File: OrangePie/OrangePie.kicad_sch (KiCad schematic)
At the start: 0 parts

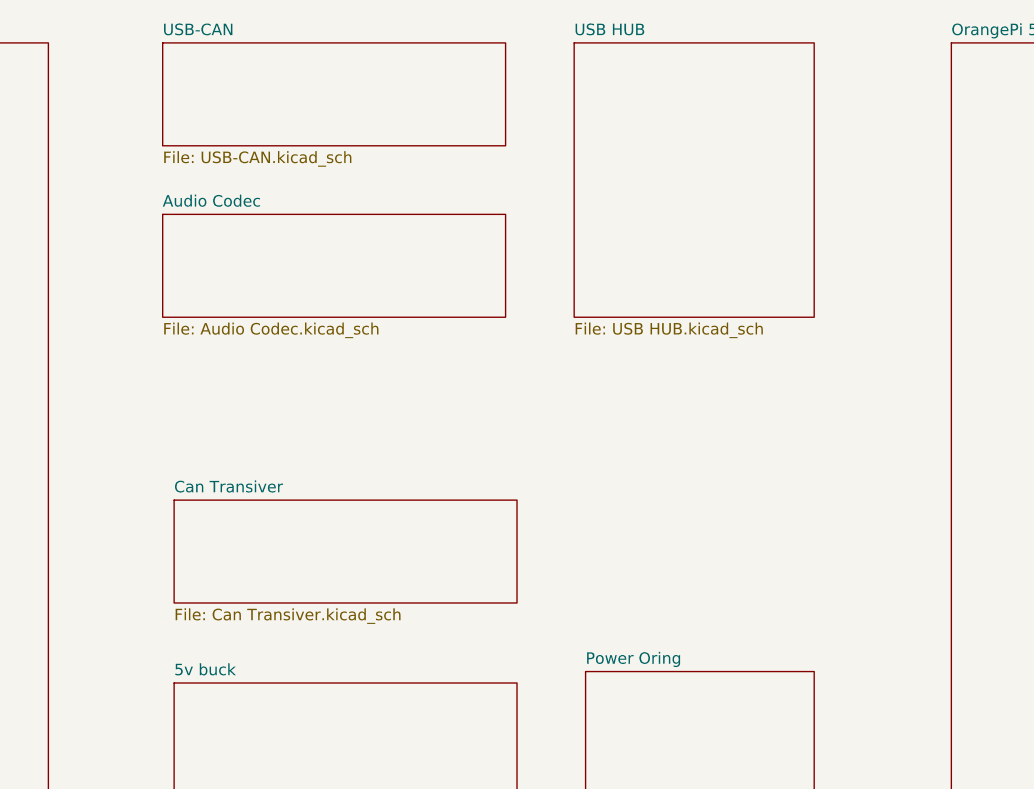
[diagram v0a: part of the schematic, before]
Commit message: Add usb hub and can tranceiver
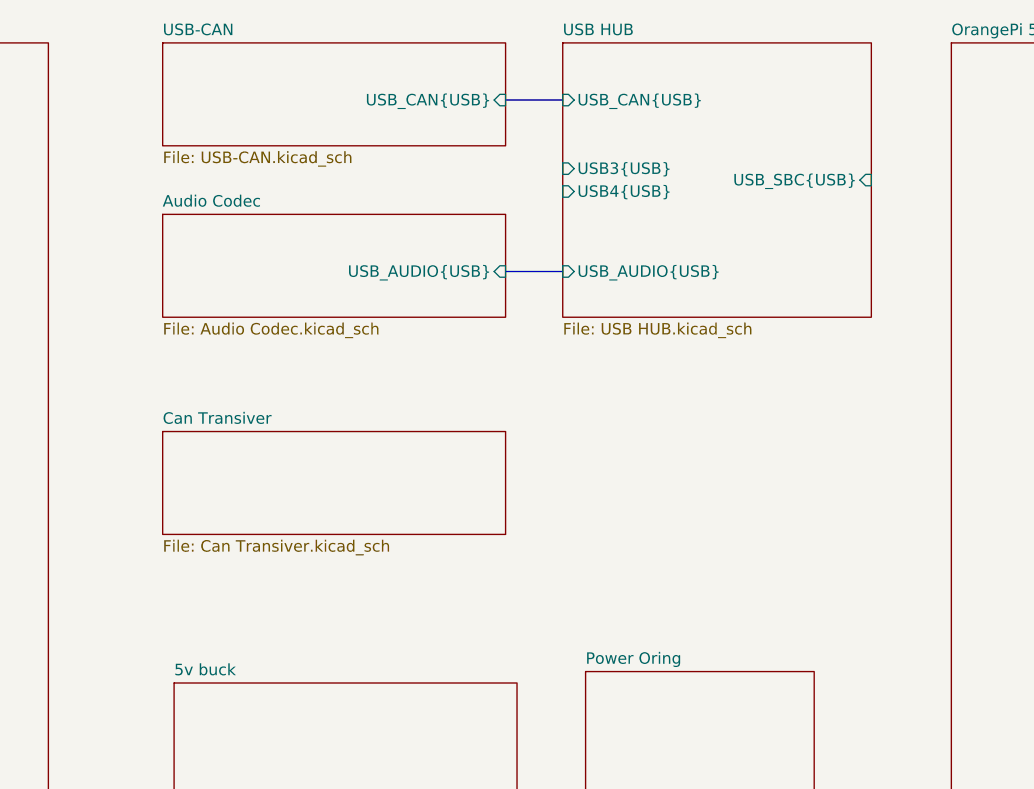
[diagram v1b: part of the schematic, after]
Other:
- sheet Audio Codec ports: added USB_AUDIO{USB}; removed none
- sheet USB HUB ports: added USB3{USB}, USB4{USB}, USB_AUDIO{USB}, USB_CAN{USB}, USB_SBC{USB}; removed none
- sheet USB-CAN ports: added USB_CAN{USB}; removed none
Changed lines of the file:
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@@
 	(generator_version "8.0")
 	(paper "A4")
+	(bus
+		(pts
+			(xy 147.32 49.53) (xy 153.67 49.53)
+		)
+		(stroke
+			(width 0)
+			(type default)
+		)
+	)
+	(bus
+		(pts
+			(xy 147.32 68.58) (xy 153.67 68.58)
+		)
+		(stroke
+			(width 0)
+			(type default)
+		)
+	)
 	(sheet
 		(at 156.21 113.03)
@@
 			)
 		)
+		(pin "USB_CAN{USB}" input
+			(at 147.32 49.53 0)
+			(effects
+				(font
+					(size 1.27 1.27)
+				)
+				(justify right)
+			)
+		)
 		(instances
 			(project "OrangePie"
@@
 	)
 	(sheet
-		(at 110.49 93.98)
+		(at 109.22 86.36)
 		(size 38.1 11.43)
 		(fields_autoplaced yes)
@@
 		)
 		(property "Sheetname" "Can Transiver"
-			(at 110.49 93.2684 0)
+			(at 109.22 85.6484 0)
 			(effects
 				(font
@@
 		)
 		(property "Sheetfile" "Can Transiver.kicad_sch"
-			(at 110.49 105.9946 0)
+			(at 109.22 98.3746 0)
 			(effects
 				(font
@@
 			)
 		)
+		(pin "USB_AUDIO{USB}" input
+			(at 147.32 68.58 0)
+			(effects
+				(font
+					(size 1.27 1.27)
+				)
+				(justify right)
+			)
+		)
 		(instances
 			(project "OrangePie"
@@
 	)
 	(sheet
-		(at 154.94 43.18)
-		(size 26.67 30.48)
+		(at 153.67 43.18)
+		(size 34.29 30.48)
 		(fields_autoplaced yes)
 		(stroke
@@
 		)
 		(property "Sheetname" "USB HUB"
-			(at 154.94 42.4684 0)
+			(at 153.67 42.4684 0)
 			(effects
 				(font
@@
 		)
 		(property "Sheetfile" "USB HUB.kicad_sch"
-			(at 154.94 74.2446 0)
-			(effects
-				(font
-					(size 1.27 1.27)
-				)
-				(justify left top)
-			)
-		)
+			(at 153.67 74.2446 0)
+			(effects
+				(font
+					(size 1.27 1.27)
+				)
+				(justify left top)
+			)
+		)
+		(pin "USB3{USB}" input
+			(at 153.67 57.15 180)
+			(effects
+				(font
+					(size 1.27 1.27)
+				)
+				(justify left)
+			)
+		)
+		(pin "USB4{USB}" input
+			(at 153.67 59.69 180)
+			(effects
+				(font
+					(size 1.27 1.27)
+				)
+				(justify left)
+			)
+		)
+		(pin "USB_SBC{USB}" input
+			(at 187.96 58.42 0)
+			(effects
+				(font
+					(size 1.27 1.27)
+				)
+				(justify right)
+			)
+		)
+		(pin "USB_AUDIO{USB}" input
+			(at 153.67 68.58 180)
+			(effects
+				(font
+					(size 1.27 1.27)
+				)
+				(justify left)
+			)
+		)
+		(pin "USB_CAN{USB}" input
+			(at 153.67 49.53 180)
+			(effects
+				(font
+					(size 1.27 1.27)
+				)
+				(justify left)
+			)
+		)

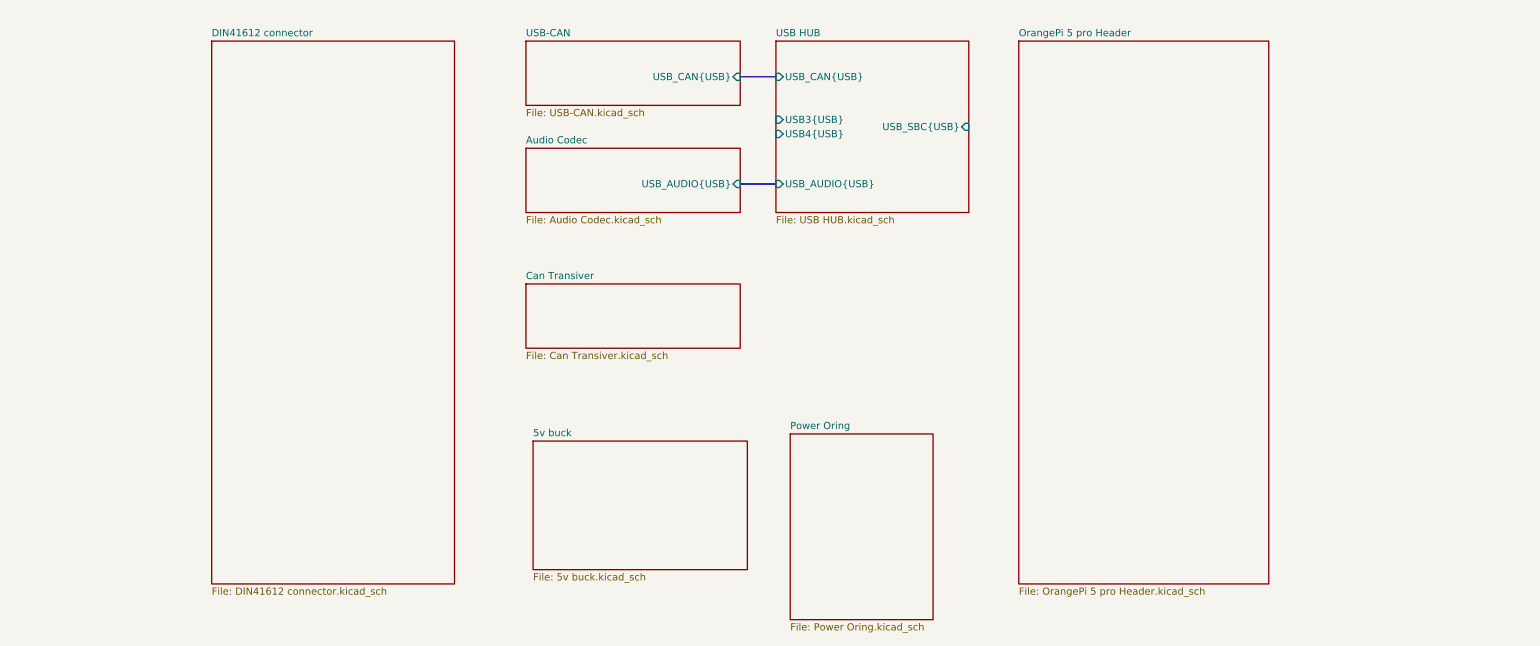
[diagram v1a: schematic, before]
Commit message: Update rest of schematic
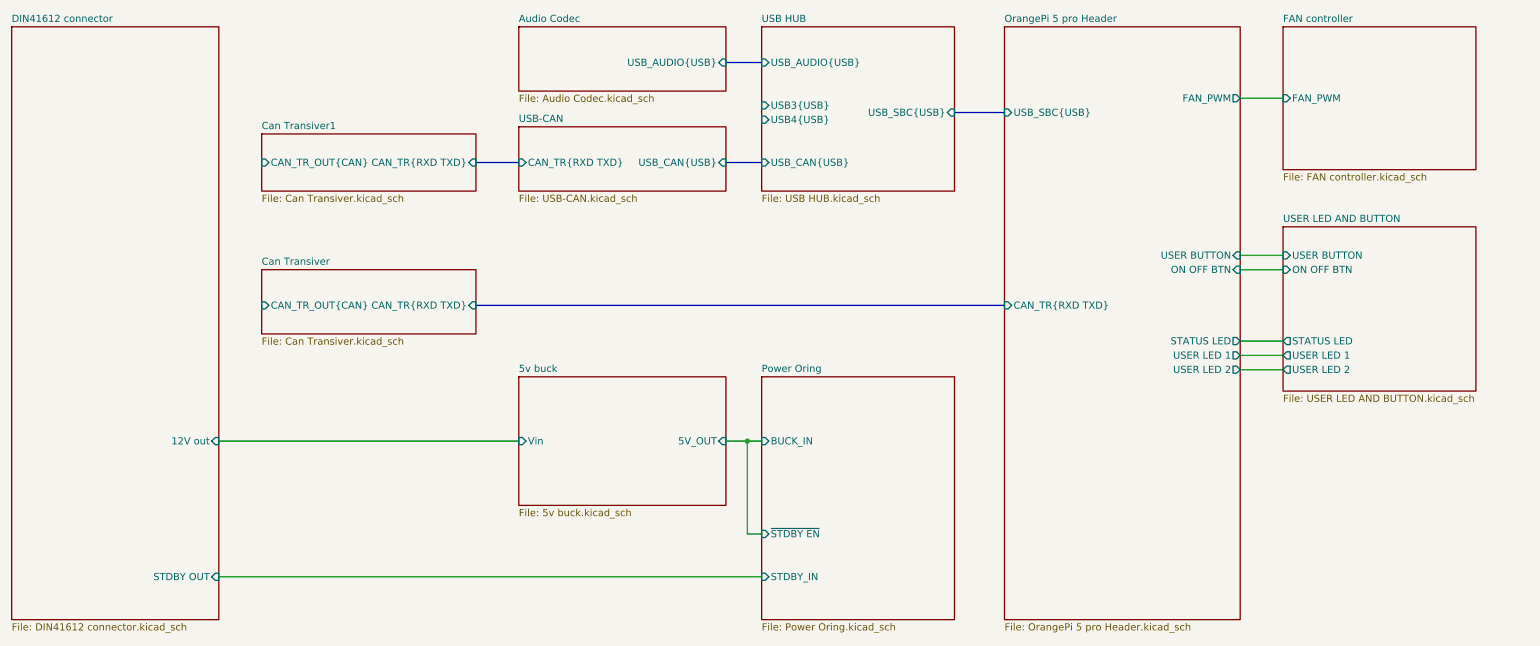
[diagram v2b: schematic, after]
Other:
- added sheet Can Transiver1 (Can Transiver.kicad_sch)
- added sheet FAN controller (FAN controller.kicad_sch)
- added sheet USER LED AND BUTTON (USER LED AND BUTTON.kicad_sch)
- sheet 5v buck ports: added 5V_OUT, Vin; removed none
- sheet Can Transiver ports: added CAN_TR_OUT{CAN}, CAN_TR{RXD TXD}; removed none
- sheet DIN41612 connector ports: added 12V out, STDBY OUT; removed none
- sheet OrangePi 5 pro Header ports: added CAN_TR{RXD TXD}, FAN_PWM, ON OFF BTN, STATUS LED, USB_SBC{USB}, USER BUTTON, USER LED 1, USER LED 2; removed none
- sheet Power Oring ports: added BUCK_IN, STDBY_IN, ~{STDBY EN}; removed none
- sheet USB-CAN ports: added CAN_TR{RXD TXD}; removed none

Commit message: Add CH340 debug
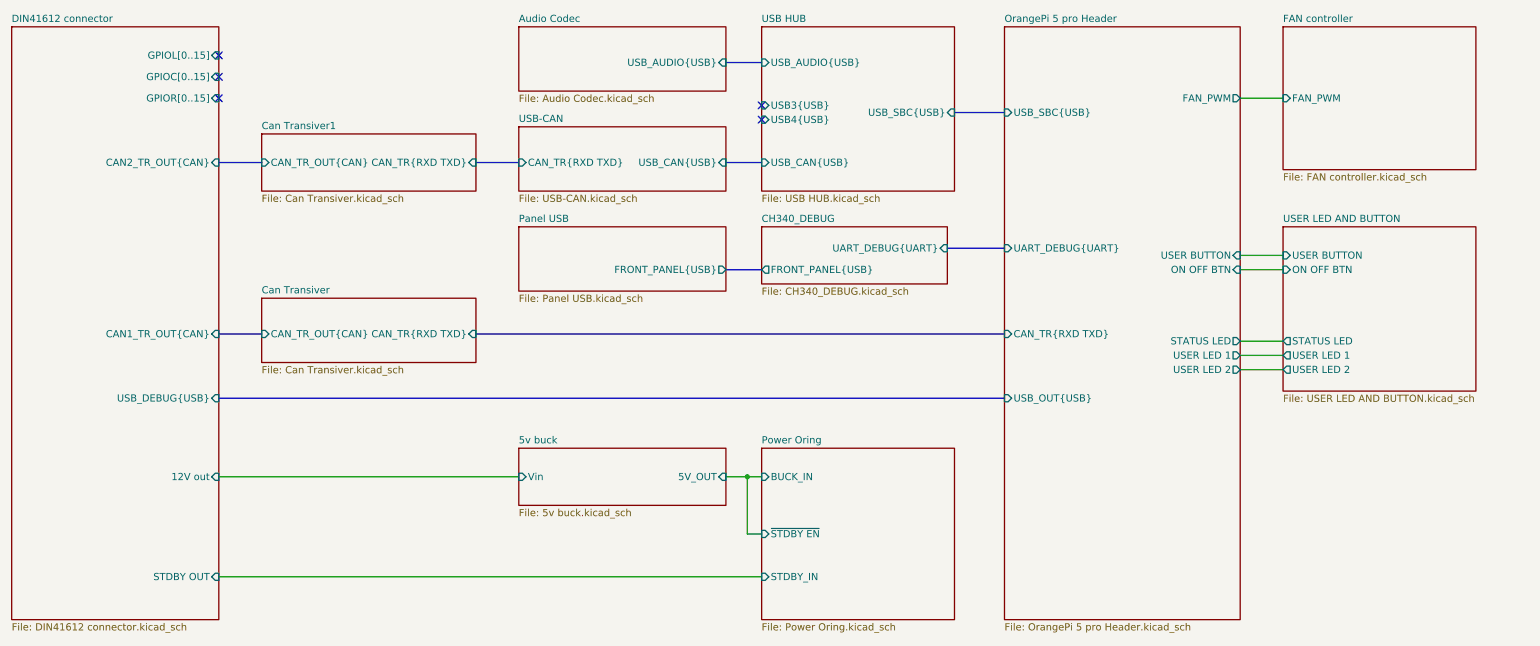
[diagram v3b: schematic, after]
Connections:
- no-connect marks 0 -> 5
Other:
- added sheet CH340_DEBUG (CH340_DEBUG.kicad_sch)
- added sheet Panel USB (Panel USB.kicad_sch)
- sheet DIN41612 connector ports: added CAN1_TR_OUT{CAN}, CAN2_TR_OUT{CAN}, GPIOC[0..15], GPIOL[0..15], GPIOR[0..15], USB_DEBUG{USB}; removed none
- sheet OrangePi 5 pro Header ports: added UART_DEBUG{UART}, USB_OUT{USB}; removed none
- company: (none) -> ModuCard System
- title: (none) -> OrangePie
